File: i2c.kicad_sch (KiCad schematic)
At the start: 18 parts, among them J5 Conn_01x04, J6 Conn_01x04, U8 ISO1541, U9 SRV05-4

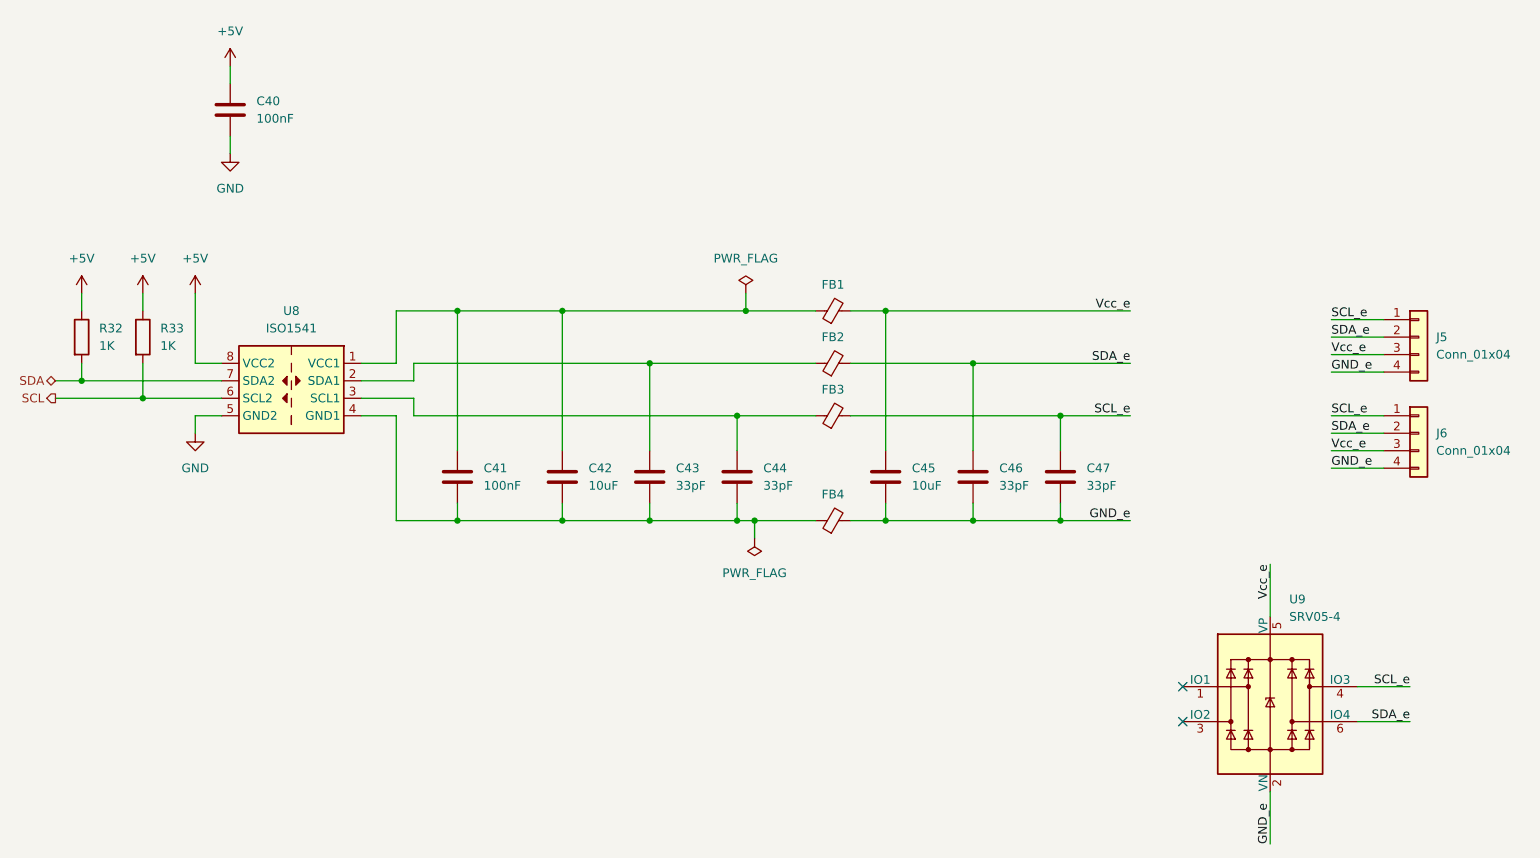
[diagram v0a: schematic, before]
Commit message: Add a lot of nice to haves
* Jumpers to bridge isolation
* I2C pullups with jumpers for input
* Labels on input connectors
* Geographic reference counts
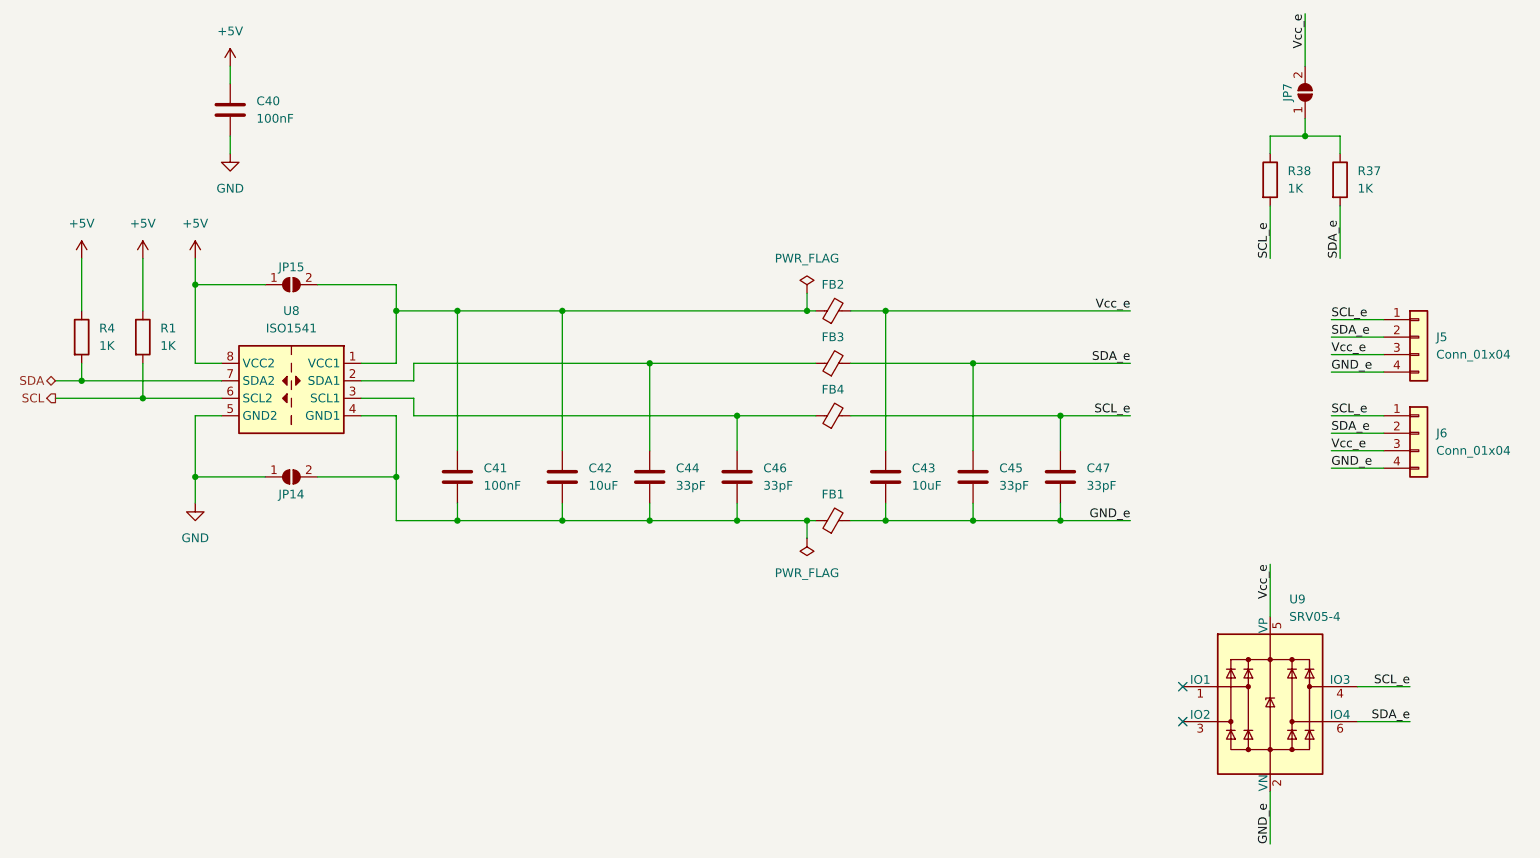
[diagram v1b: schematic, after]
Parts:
- added JP14, JP15, JP7: SolderJumper_2_Open, Jumper:SolderJumper-2_P1.3mm_Open_TrianglePad1.0x1.5mm, symbol Jumper:SolderJumper_2_Open
- added R37, R38: 1K, Resistor_SMD:R_0603_1608Metric, symbol Device:R
- renumbered C45 to C43, C43 to C44, C46 to C45, C44 to C46, FB4 to FB1, FB1 to FB2, FB2 to FB3, FB3 to FB4, R33 to R1, R32 to R4
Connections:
- net +5V: now also JP15.1 (A)
- net GND: now also JP14.1 (A)
- net SCL_e: now also R38.2
- net SDA_e: now also R37.2
- net Vcc_e: now also JP7.2 (B)
- net at C41.1, C42.1, FB2.1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: now also JP15.2 (B)
- net at C41.2, C42.2, C44.2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: now also JP14.2 (B)
- new net: JP7.1 (A), R37.1, R38.1

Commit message: Add LCSC order numbers to more easily order at JLCPCB
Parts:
- C40, C41: LCSC Part # (none) -> C14663
- C42, C43: LCSC Part # (none) -> C13585
- C44, C45, C46, C47: LCSC Part # (none) -> C1663
- FB1, FB2, FB3, FB4: value BLM15HB221 -> FerriteBead; LCSC Part # (none) -> C1002
- R1, R37, R38, R4: LCSC Part # (none) -> C21190
- U8: LCSC Part # (none) -> C143028
- U9: LCSC Part # (none) -> C85364
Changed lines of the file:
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@@
+      (effects (font (size 1.27 1.27)) hide)
+    )
+    (property "LCSC Part #" "C1663" (id 4) (at 181.61 85.09 0)
       (effects (font (size 1.27 1.27)) hide)
     )
@@
       (effects (font (size 1.27 1.27)) hide)
     )
+    (property "LCSC Part #" "C14663" (id 4) (at 106.68 85.09 0)
+      (effects (font (size 1.27 1.27)) hide)
+    )
     (pin "1")
     (pin "2")
@@
     )
     (property "Datasheet" "~" (id 3) (at 194.31 85.09 0)
+      (effects (font (size 1.27 1.27)) hide)
+    )
+    (property "LCSC Part #" "C1663" (id 4) (at 194.31 85.09 0)
       (effects (font (size 1.27 1.27)) hide)
     )
@@
     )
     (property "Datasheet" "http://www.onsemi.com/pub/Collateral/SRV05-4-D.PDF" (id 3) (at 224.79 118.11 0)
+      (effects (font (size 1.27 1.27)) hide)
+    )
+    (property "LCSC Part #" "C85364" (id 4) (at 224.79 118.11 0)
       (effects (font (size 1.27 1.27)) hide)
     )
@@
       (effects (font (size 1.27 1.27)) hide)
     )
+    (property "LCSC Part #" "C1663" (id 4) (at 134.62 85.09 0)
+      (effects (font (size 1.27 1.27)) hide)
+    )
     (pin "1")
     (pin "2")
@@
     )
     (property "Datasheet" "~" (id 3) (at 224.79 41.91 0)
+      (effects (font (size 1.27 1.27)) hide)
+    )
+    (property "LCSC Part #" "C21190" (id 4) (at 224.79 41.91 0)
       (effects (font (size 1.27 1.27)) hide)
     )
@@
     (in_bom yes) (on_board yes) (fields_autoplaced)
     (property "Reference" "FB2" (id 0) (at 161.2519 57.15 90))
-    (property "Value" "BLM15HB221" (id 1) (at 161.2519 57.15 90)
+    (property "Value" "FerriteBead" (id 1) (at 161.2519 57.15 90)
       (effects (font (size 1.27 1.27)) hide)
     )
@@
     )
     (property "Datasheet" "~" (id 3) (at 161.29 60.96 0)
+      (effects (font (size 1.27 1.27)) hide)
+    )
+    (property "LCSC Part #" "C1002" (id 4) (at 161.29 60.96 0)
       (effects (font (size 1.27 1.27)) hide)
     )
@@
       (effects (font (size 1.27 1.27)) hide)
     )
+    (property "LCSC Part #" "C21190" (id 4) (at 52.07 64.77 0)
+      (effects (font (size 1.27 1.27)) hide)
+    )
     (pin "1")
     (pin "2")
@@
       (effects (font (size 1.27 1.27)) hide)
     )
+    (property "LCSC Part #" "C13585" (id 4) (at 121.92 85.09 0)
+      (effects (font (size 1.27 1.27)) hide)
+    )
     (pin "1")
     (pin "2")
@@
     (in_bom yes) (on_board yes) (fields_autoplaced)
     (property "Reference" "FB3" (id 0) (at 161.2519 64.77 90))
-    (property "Value" "BLM15HB221" (id 1) (at 161.2519 64.77 90)
+    (property "Value" "FerriteBead" (id 1) (at 161.2519 64.77 90)
       (effects (font (size 1.27 1.27)) hide)
     )
@@
     )
     (property "Datasheet" "~" (id 3) (at 161.29 68.58 0)
+      (effects (font (size 1.27 1.27)) hide)
+    )
+    (property "LCSC Part #" "C1002" (id 4) (at 161.29 68.58 0)
       (effects (font (size 1.27 1.27)) hide)
     )
@@
     )
     (property "Datasheet" "http://www.ti.com/lit/ds/symlink/iso1541.pdf" (id 3) (at 82.55 69.85 0)
+      (effects (font (size 1.27 1.27)) hide)
+    )
+    (property "LCSC Part #" "C143028" (id 4) (at 82.55 71.12 0)
       (effects (font (size 1.27 1.27)) hide)
     )
@@
       (effects (font (size 1.27 1.27)) hide)
     )
+    (property "LCSC Part #" "C14663" (id 4) (at 73.66 31.75 0)
+      (effects (font (size 1.27 1.27)) hide)
+    )
     (pin "1")
     (pin "2")
@@
       (effects (font (size 1.27 1.27)) hide)
     )
+    (property "LCSC Part #" "C21190" (id 4) (at 234.95 41.91 0)
+      (effects (font (size 1.27 1.27)) hide)
+    )
     (pin "1")
     (pin "2")
@@
     )
     (property "Datasheet" "~" (id 3) (at 168.91 85.09 0)
+      (effects (font (size 1.27 1.27)) hide)
+    )
+    (property "LCSC Part #" "C13585" (id 4) (at 168.91 85.09 0)
       (effects (font (size 1.27 1.27)) hide)
     )
@@
     (in_bom yes) (on_board yes) (fields_autoplaced)
     (property "Reference" "FB4" (id 0) (at 161.2519 72.39 90))
-    (property "Value" "BLM15HB221" (id 1) (at 161.2519 72.39 90)
+    (property "Value" "FerriteBead" (id 1) (at 161.2519 72.39 90)
       (effects (font (size 1.27 1.27)) hide)
     )
@@
       (effects (font (size 1.27 1.27)) hide)
     )
+    (property "LCSC Part #" "C1002" (id 4) (at 161.29 76.2 0)
+      (effects (font (size 1.27 1.27)) hide)
+    )
     (pin "1")
     (pin "2")
@@
       (effects (font (size 1.27 1.27)) hide)
     )
+    (property "LCSC Part #" "C1663" (id 4) (at 147.32 85.09 0)
+      (effects (font (size 1.27 1.27)) hide)
+    )
     (pin "1")
     (pin "2")
@@
       (effects (font (size 1.27 1.27)) hide)
     )
+    (property "LCSC Part #" "C21190" (id 4) (at 60.96 64.77 0)
+      (effects (font (size 1.27 1.27)) hide)
+    )
     (pin "1")
     (pin "2")
@@
     (in_bom yes) (on_board yes) (fields_autoplaced)
     (property "Reference" "FB1" (id 0) (at 161.2519 87.63 90))
-    (property "Value" "BLM15HB221" (id 1) (at 161.2519 87.63 90)
+    (property "Value" "FerriteBead" (id 1) (at 161.2519 87.63 90)
       (effects (font (size 1.27 1.27)) hide)
     )
@@
       (effects (font (size 1.27 1.27)) hide)
     )
+    (property "LCSC Part #" "C1002" (id 4) (at 161.29 91.44 0)
+      (effects (font (size 1.27 1.27)) hide)
+    )

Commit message: Remove PCB only parts from BOM
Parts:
- JP14, JP15, JP7: now left out of the parts list
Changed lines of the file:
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@@
   )
   (symbol (lib_id "Jumper:SolderJumper_2_Open") (at 82.55 57.15 0) (unit 1)
-    (in_bom yes) (on_board yes)
+    (in_bom no) (on_board yes)
     (property "Reference" "JP15" (id 0) (at 82.55 54.61 0))
     (property "Value" "SolderJumper_2_Open" (id 1) (at 81.2801 59.69 90)
@@
   )
   (symbol (lib_id "Jumper:SolderJumper_2_Open") (at 82.55 85.09 0) (unit 1)
-    (in_bom yes) (on_board yes)
+    (in_bom no) (on_board yes)
     (property "Reference" "JP14" (id 0) (at 82.55 87.63 0))
     (property "Value" "SolderJumper_2_Open" (id 1) (at 81.2801 87.63 90)
@@
   )
   (symbol (lib_id "Jumper:SolderJumper_2_Open") (at 229.87 29.21 90) (unit 1)
-    (in_bom yes) (on_board yes)
+    (in_bom no) (on_board yes)
     (property "Reference" "JP7" (id 0) (at 227.33 29.21 0))
     (property "Value" "SolderJumper_2_Open" (id 1) (at 232.41 30.4799 90)

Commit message: Add JLCPCB rotation offsets
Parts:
- U8: JLCPCB Rotation Offset (none) -> -90
- U9: JLCPCB Rotation Offset (none) -> 180
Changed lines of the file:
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@@
+      (effects (font (size 1.27 1.27)) hide)
+    )
+    (property "JLCPCB Rotation Offset" "180" (id 5) (at 224.79 118.11 0)
       (effects (font (size 1.27 1.27)) hide)
     )
@@
       (effects (font (size 1.27 1.27)) hide)
     )
+    (property "JLCPCB Rotation Offset" "-90" (id 5) (at 82.55 71.12 0)
+      (effects (font (size 1.27 1.27)) hide)
+    )

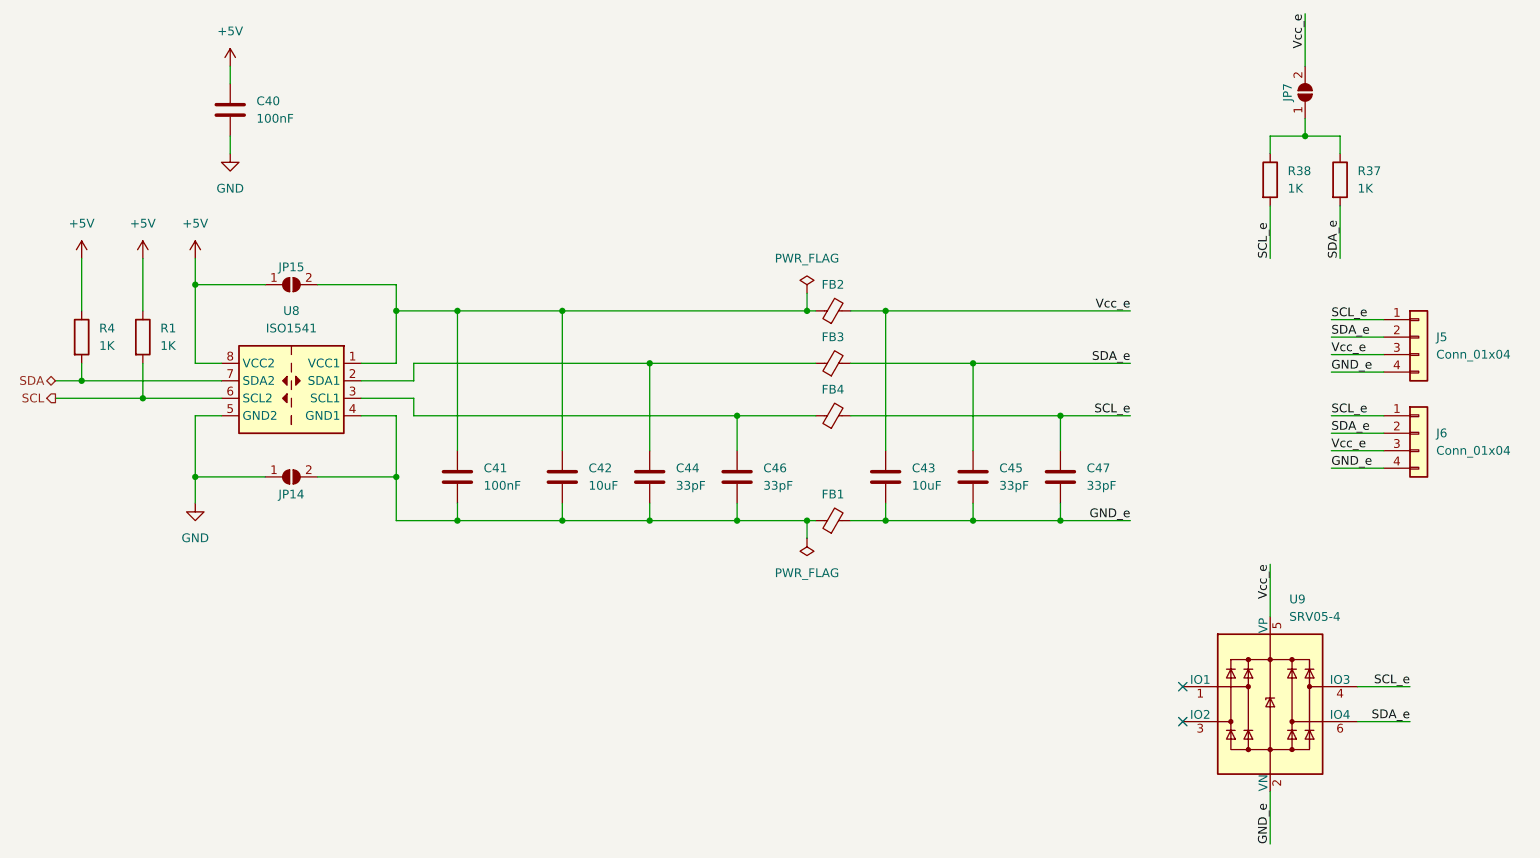
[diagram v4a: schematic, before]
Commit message: Shrink board and reduce features to reduce price
* Shrink to 100mm x 50mm
* Remove voltage regulator and use Stemma Power instead
* Remove isolation (is easier to add outside when needed)
* Remove reverse indicators to save space
* Remove I2C pullups as they are no longer needed
* Fix A2 of EEPROM and Temperature sensor to 0 to save space
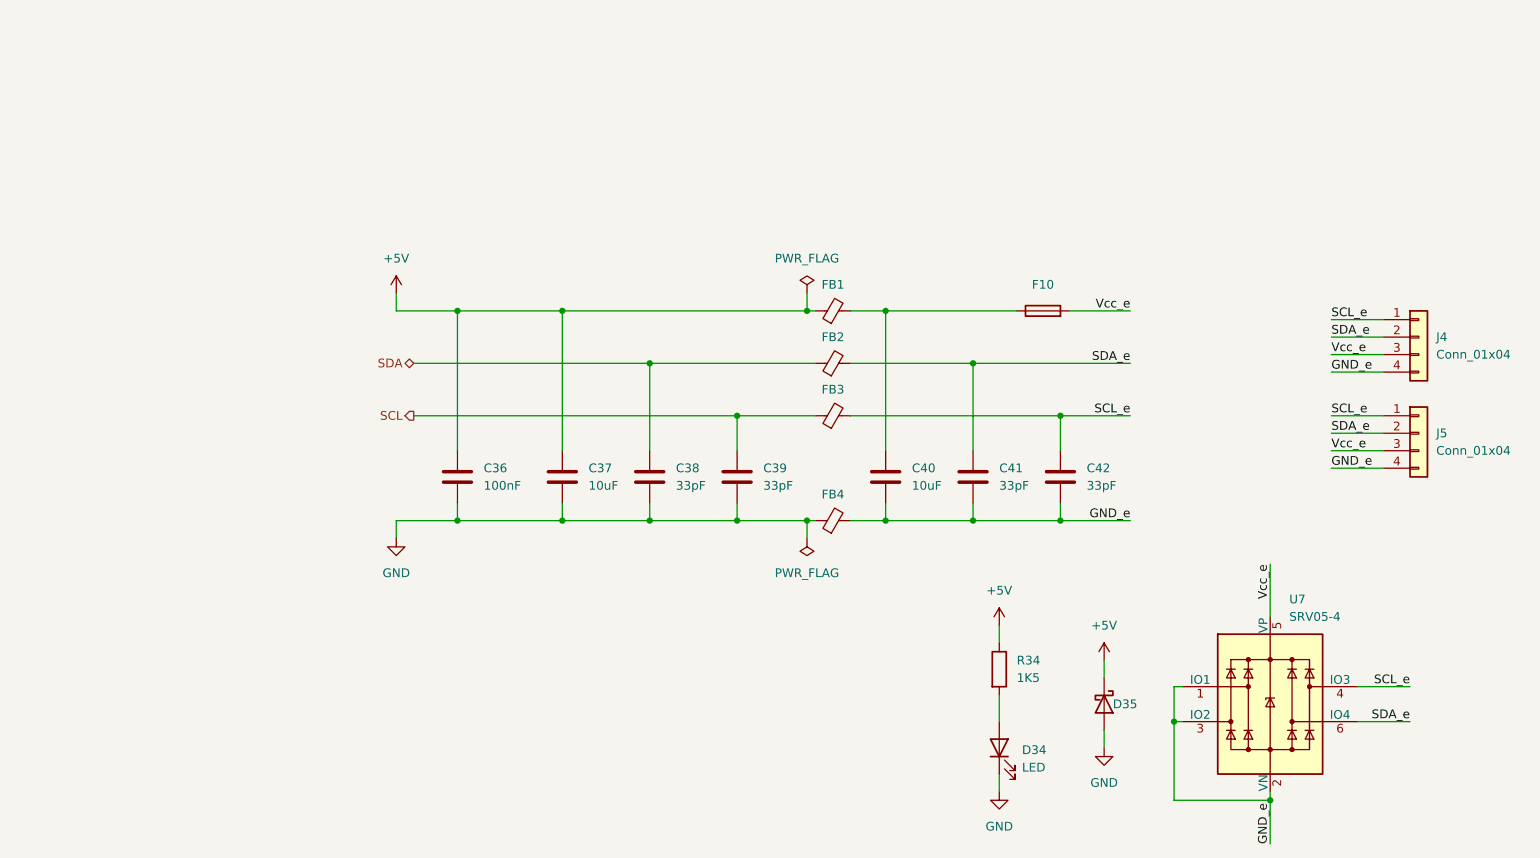
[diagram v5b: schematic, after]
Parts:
- removed C40: 100nF, Capacitor_SMD:C_0603_1608Metric, symbol Device:C
- removed JP14, JP15, JP7: SolderJumper_2_Open, Jumper:SolderJumper-2_P1.3mm_Open_TrianglePad1.0x1.5mm, symbol Jumper:SolderJumper_2_Open
- removed R1, R37, R38, R4: 1K, Resistor_SMD:R_0603_1608Metric, symbol Device:R
- removed U8: ISO1541, Package_SO:SOIC-8_3.9x4.9mm_P1.27mm, symbol Isolator:ISO1541
- added D34: LED, LED_SMD:LED_0603_1608Metric, symbol Device:LED
- added D35: PMEG4010BEA, Diode_SMD:D_SOD-323F, symbol Device:D_Schottky
- added F10: 1206L016WR, Fuse:Fuse_1206_3216Metric_Pad1.42x1.75mm_HandSolder, symbol Device:Fuse
- added R34: 1K5, Resistor_SMD:R_0603_1608Metric, symbol Device:R
- renumbered C41 to C36, C42 to C37, C44 to C38, C46 to C39, C43 to C40, C45 to C41, C47 to C42, FB2 to FB1, FB3 to FB2, FB4 to FB3, FB1 to FB4, J5 to J4, J6 to J5, U9 to U7
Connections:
- net +5V: now also C36.1, C37.1, FB1.1, D35.1 (K), R34.1
- net GND: now also C36.2, C37.2, C38.2, C39.2, FB4.1, D34.1 (K), D35.2 (A)
- net GND_e: now also U7.1 (IO1), U7.3 (IO2)
- net SCL: now also C39.1, FB3.1
- net SDA: now also C38.1, FB2.1
- net Vcc_e: now also F10.2; no longer C40.1, FB1.2
- new net: D34.2 (A), R34.2
- new net: C40.1, F10.1, FB1.2
- no-connect marks 2 -> 0
